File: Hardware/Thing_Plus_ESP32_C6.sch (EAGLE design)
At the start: 61 parts, among them J1 THING_PLUS_LOGICAL, J4 QWIIC_RIGHT_ANGLE, J5 MICRO-SDFRICTION, Q1 20V/4.2A/52mΩ/1.4W, Q2 20V/4.2A/52mΩ/1.4W, U1 ESP32-C6-WROOM-1-NARROW, U2 RT9080-33GJ5, U3 MCP73831, U4 MAX17048

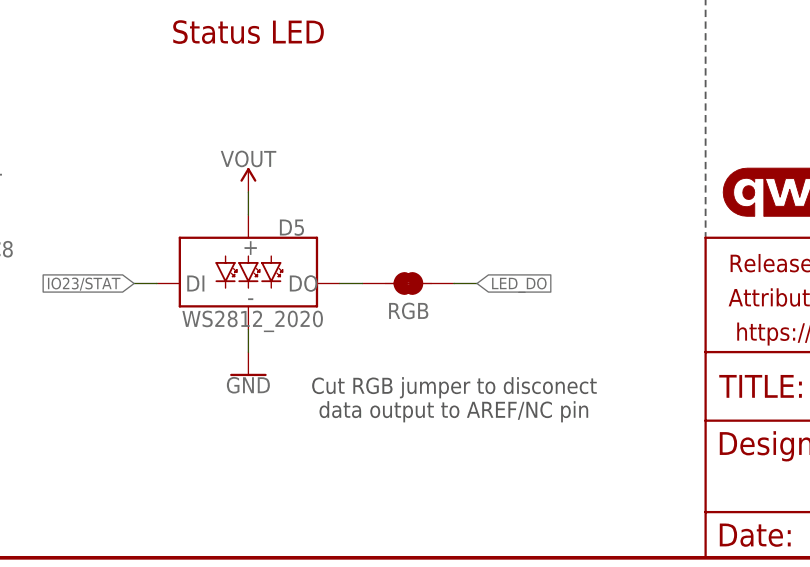
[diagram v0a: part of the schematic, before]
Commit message: Change RGB jumper to NO
Won't violate the form factor standard by default this time!
Also update panel files
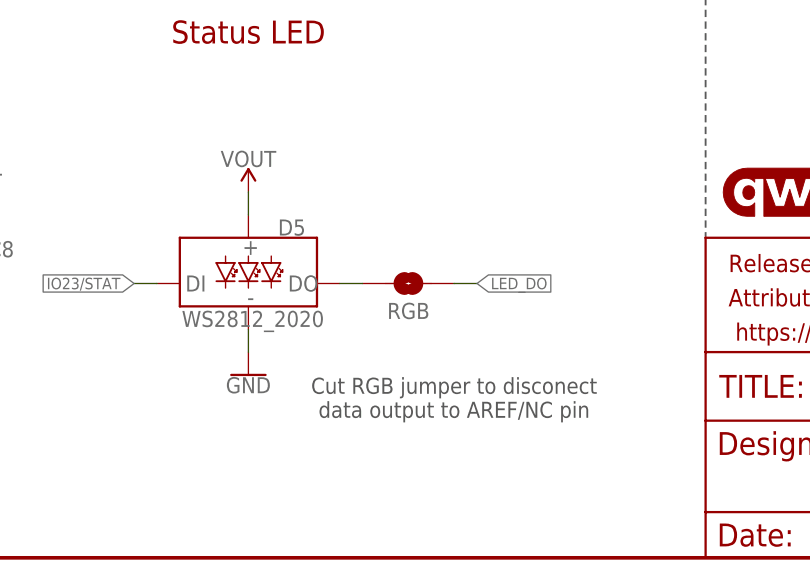
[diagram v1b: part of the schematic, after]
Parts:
- RGB: value JUMPER-SMT_2_NC_TRACE_SILK -> JUMPER-SMT_2_NO_SILK; device SparkFun-Jumpers:JUMPER-SMT_2_NC_TRACE_SILK -> SparkFun-Jumpers:JUMPER-SMT_2_NO_SILK
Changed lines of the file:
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@@
 <part name="SD_DET" library="SparkFun-Jumpers" deviceset="JUMPER-SMT_2_NC_TRACE" device="_SILK" package3d_urn="urn:adsk.eagle:package:39281/1"/>
 <part name="MEAS" library="SparkFun-Jumpers" deviceset="JUMPER-COMBO_2_NC_TRACE" device=""/>
-<part name="RGB" library="SparkFun-Jumpers" deviceset="JUMPER-SMT_2_NC_TRACE" device="_SILK" package3d_urn="urn:adsk.eagle:package:39281/1"/>
+<part name="RGB" library="SparkFun-Jumpers" deviceset="JUMPER-SMT_2_NO" device="_SILK" package3d_urn="urn:adsk.eagle:package:39279/1"/>
 <part name="R5" library="SparkFun-Resistors" deviceset="100KOHM" device="-0603-1/10W-1%" value="100k"/>
 <part name="H3" library="SparkFun-Hardware" deviceset="STAND-OFF" device=""/>

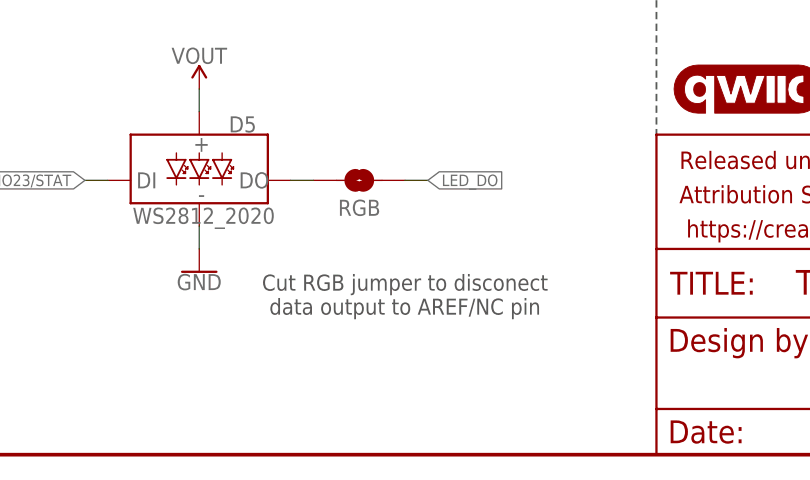
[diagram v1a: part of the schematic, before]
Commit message: Fix schematic note about RGB jumper
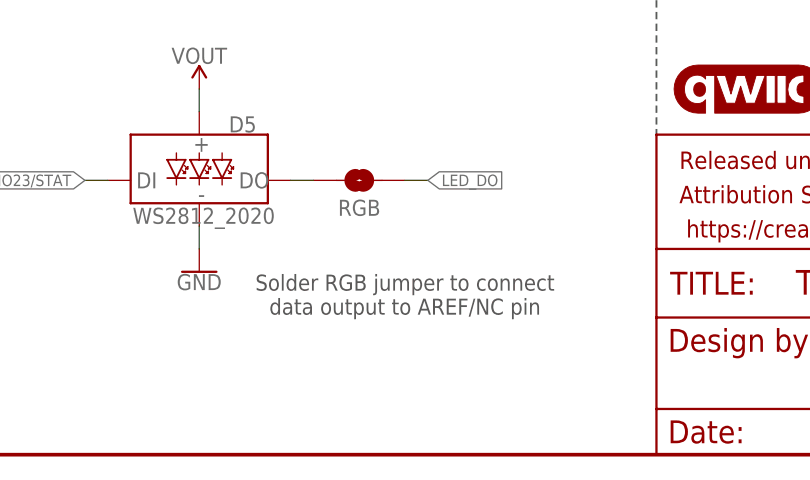
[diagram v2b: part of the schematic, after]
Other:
- note added: "Solder RGB jumper to connect data output to AREF/NC pin"
- note removed: "Cut RGB jumper to disconect data output to AREF/NC pin"
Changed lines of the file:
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@@
 <text x="360.68" y="144.78" size="1.778" layer="97" font="vector" align="center">Cut SD_DET jumper to disable
 uSD card insertion detection</text>
-<text x="302.26" y="17.78" size="1.778" layer="97" font="vector" align="center">Cut RGB jumper to disconect
+<text x="302.26" y="17.78" size="1.778" layer="97" font="vector" align="center">Solder RGB jumper to connect
 data output to AREF/NC pin</text>
 <wire x1="228.6" y1="213.36" x2="330.2" y2="213.36" width="0.2032" layer="97" style="longdash"/>

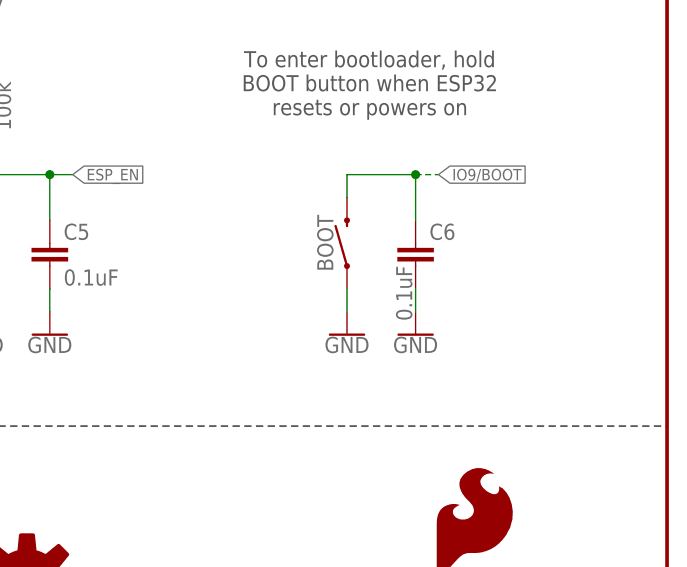
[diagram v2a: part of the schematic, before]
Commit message: Change C6 to DNP
Rise time was slow, causing chip to run bootloader instead of booting from flash
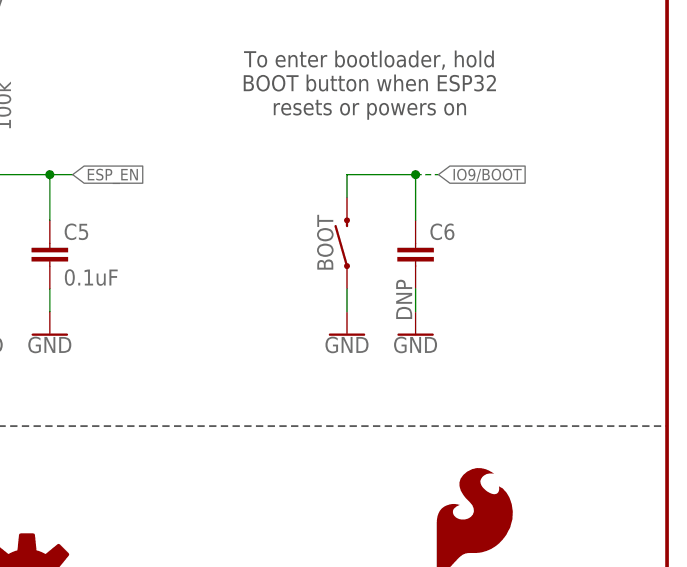
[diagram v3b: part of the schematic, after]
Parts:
- C6: value 0.1uF -> DNP
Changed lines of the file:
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@@
 <part name="SUPPLY12" library="SparkFun-PowerSymbols" deviceset="3.3V" device=""/>
 <part name="GND21" library="SparkFun-PowerSymbols" deviceset="GND" device=""/>
-<part name="C6" library="SparkFun-Capacitors" deviceset="0.1UF" device="-0603-25V-(+80/-20%)" value="0.1uF"/>
+<part name="C6" library="SparkFun-Capacitors" deviceset="0.1UF" device="-0603-25V-(+80/-20%)" value="DNP">
+<attribute name="PROD_ID" value=""/>
+</part>
 <part name="GND22" library="SparkFun-PowerSymbols" deviceset="GND" device=""/>
 <part name="U2" library="SparkFun-IC-Power" deviceset="V_REG_RT9080" device="" value="RT9080-33GJ5"/>
